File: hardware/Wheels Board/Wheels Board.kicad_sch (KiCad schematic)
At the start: 28 parts, among them J1 53307-2471, J2 MX150_02x04_Vertical, J4 Conn_01x08_Socket, U1 XIAO-ESP32-S3-SMD, U2 ASM330LHHTR, U5 TLV9002QDRQ1

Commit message: concepts of revA layout
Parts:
- removed J2: MX150_02x04_Vertical, UTSVT_Connectors:CONN_SD-75757-002_2X04_F16p09_MOL, symbol utsvt_connectors:MX150_02x04_Vertical
- removed J4: Conn_01x08_Socket, Connector_PinHeader_2.54mm:PinHeader_1x08_P2.54mm_Vertical, symbol Connector:Conn_01x08_Socket
- added J3: Conn_02x04_Counter_Clockwise, Connector_PinHeader_2.54mm:PinHeader_2x04_P2.54mm_Vertical, symbol Connector_Generic:Conn_02x04_Counter_Clockwise
- added J4: 757571121, mx150_2x2:CONN_SD-75757-002_2X02_F11p20_MOL, symbol mx150_2x2:757571121
- renumbered TP_GND2 to HALL_GND1, TP_OUT1 to HALL_OUT1, TP_5V2 to HALL_PWR1
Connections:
- net +24V: now also J4.1
- net CAN_H: now also J4.2
- net CAN_L: now also J4.3
- net ESP_SPI_CLK: now also J3.2 (Pin_2)
- net ESP_SPI_MISO: now also J3.4 (Pin_4)
- net ESP_SPI_MOSI: now also J3.3 (Pin_3)
- net ESP_SPI_SS: now also J3.1 (Pin_1)
- net GND: now also J4.4
- net IMU_SPI_CLK: now also J3.7 (Pin_7)
- net IMU_SPI_MISO: now also J3.5 (Pin_5)
- net IMU_SPI_MOSI: now also J3.6 (Pin_6)
- net IMU_SPI_SS: now also J3.8 (Pin_8)
- no-connect marks 22 -> 18
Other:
- note added: "MX150_CONNECTOR"
- note removed: "CONNECTOR"

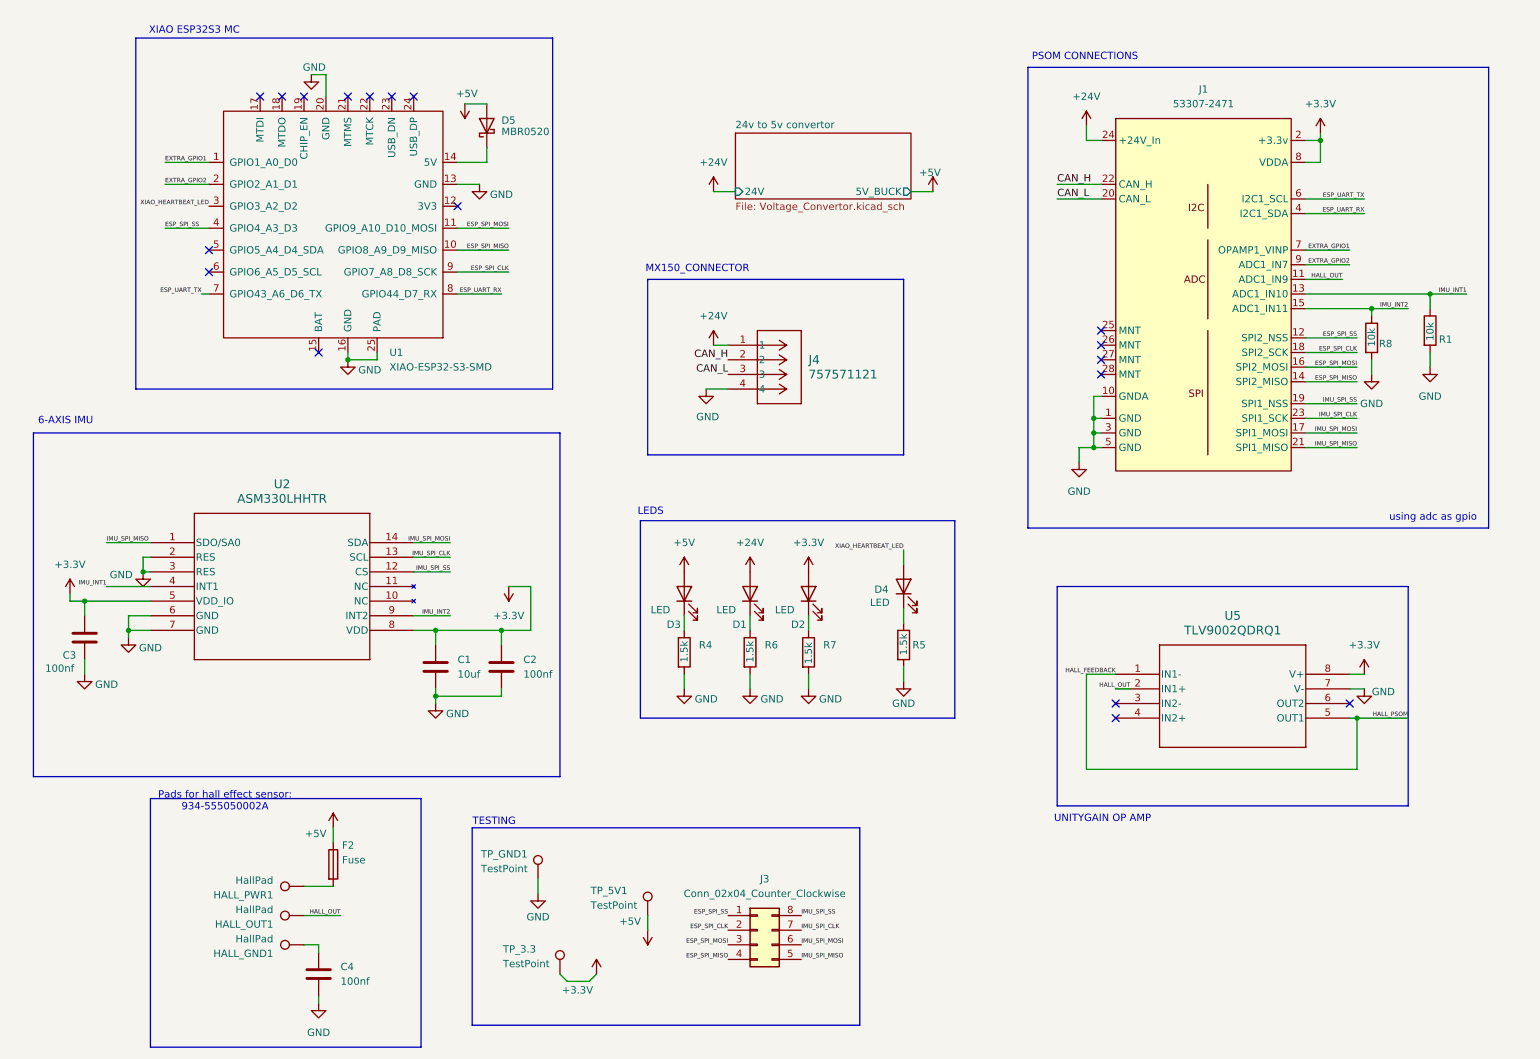
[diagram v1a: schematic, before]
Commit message: review council changes, layout not finalized
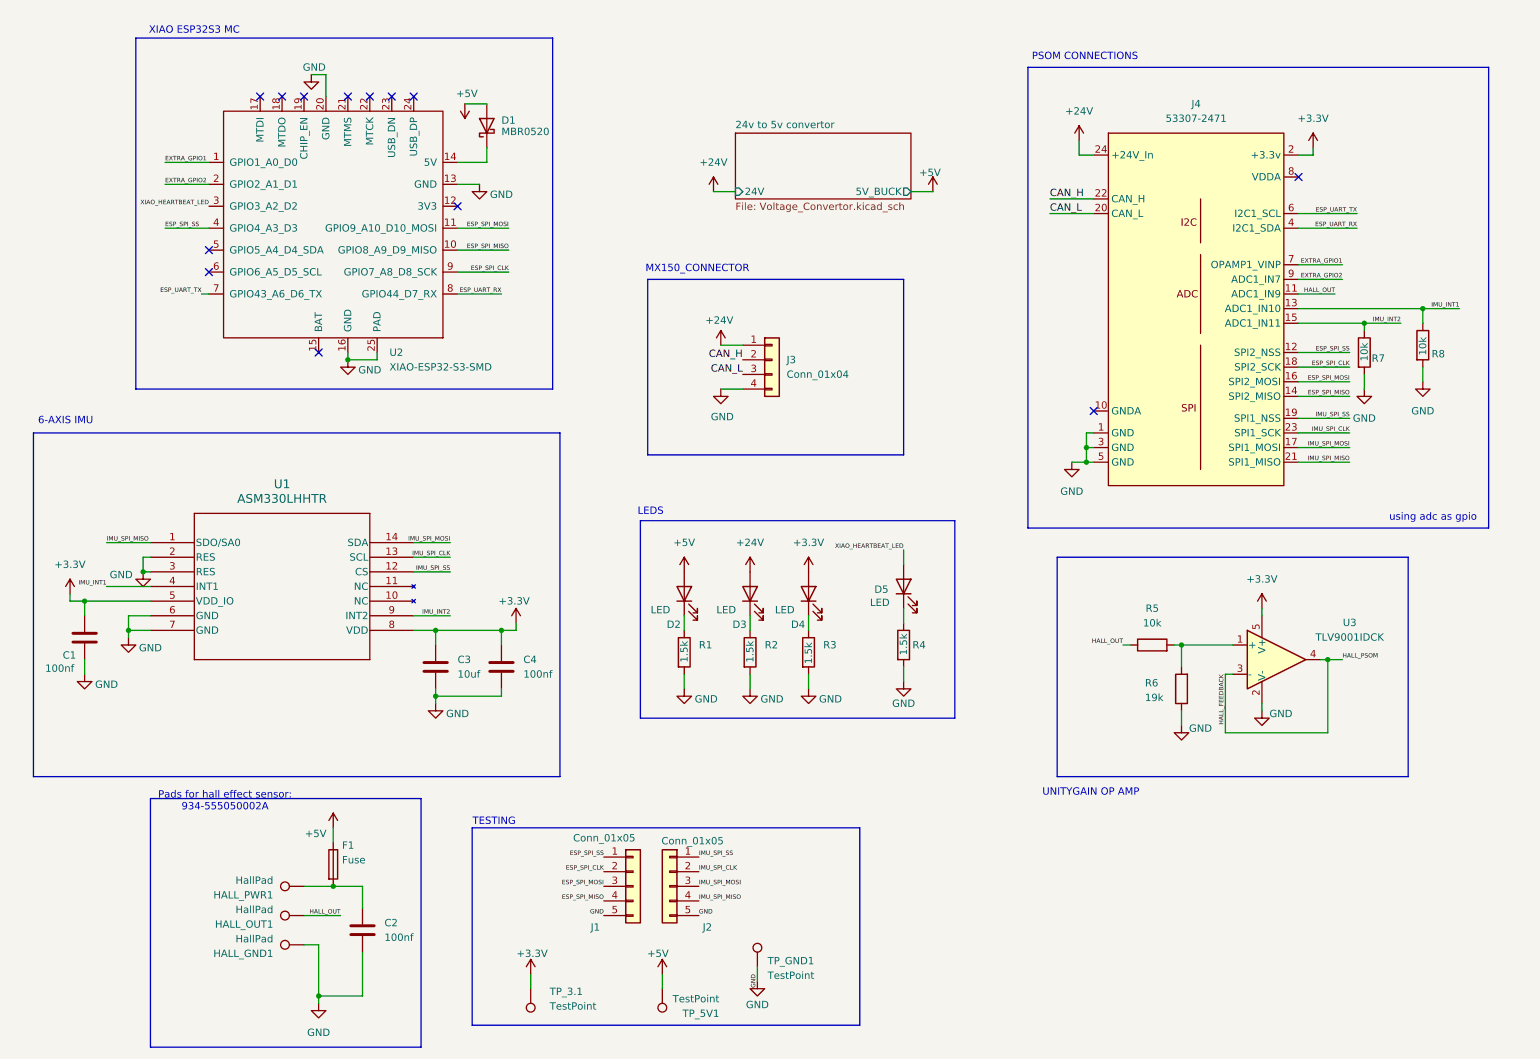
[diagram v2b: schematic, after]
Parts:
- removed C4: 100nf, Capacitor_SMD:C_0603_1608Metric_Pad1.08x0.95mm_HandSolder, symbol Device:C
- removed J1: 53307-2471, UTSVT_Connectors:PeripheralSOM, symbol utsvt_connectors:PeripheralSOMConnector
- removed J3: Conn_02x04_Counter_Clockwise, Connector_PinHeader_2.54mm:PinHeader_2x04_P2.54mm_Vertical, symbol Connector_Generic:Conn_02x04_Counter_Clockwise
- removed J4: 757571121, mx150_2x2:CONN_SD-75757-002_2X02_F11p20_MOL, symbol mx150_2x2:757571121
- removed R1: 10k, Resistor_SMD:R_0603_1608Metric_Pad0.98x0.95mm_HandSolder, symbol Device:R
- removed U5: TLV9002QDRQ1, TLV9002QDRQ1:SOIC8_D_TEX, symbol TLV9002QDRQ1(Op-Amp):TLV9002QDRQ1
- added C2: 100nf, Capacitor_SMD:C_0603_1608Metric_Pad1.08x0.95mm_HandSolder, symbol Device:C
- added J1, J2: Conn_01x05, Connector_PinHeader_1.00mm:PinHeader_1x05_P1.00mm_Vertical_SMD_Pin1Left, symbol Connector_Generic:Conn_01x05
- added J3: Conn_01x04, mx150_2x2:CONN_SD-75757-002_2X02_F11p20_MOL, symbol Connector_Generic:Conn_01x04
- added J4: 53307-2471, UTSVT_Connectors:PeripheralSOM, symbol utsvt_connectors:PeripheralSOMConnector
- added R5, R7: 10k, Resistor_SMD:R_0603_1608Metric_Pad0.98x0.95mm_HandSolder, symbol Device:R
- added R6: 19k, Resistor_SMD:R_0603_1608Metric_Pad0.98x0.95mm_HandSolder, symbol Device:R
- added U3: TLV9001IDCK, Package_TO_SOT_SMD:SOT-353_SC-70-5, symbol Amplifier_Operational:TLV9001IDCK
- C1: renamed from C3; P/N (none) -> MLASH168SB7104KTNA01
- C4: renamed from C2; P/N (none) -> MLASH168SB7104KTNA01
- D1: renamed from D5; P/N (none) -> MP01EA06
- U1: renamed from U2; P/N (none) -> ASM330LHHTR
- U2: renamed from U1; footprint XIAO-ESP32S3-SMD:XIAO-ESP32S3-SMD -> XIAO-ESP32S3:XIAO-ESP32S3-DIP; P/N (none) -> 113991114
- renumbered C1 to C3, D3 to D2, D1 to D3, D2 to D4, D4 to D5, F2 to F1, R4 to R1, R6 to R2, R7 to R3, R5 to R4, TP_3.3 to TP_3.1
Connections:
- net +24V: now also J3.1 (Pin_1), J4.24 (+24V_In)
- net +3.3V: now also J4.2 (+3.3v), U3.5 (V+)
- net CAN_H: now also J3.2 (Pin_2), J4.22 (CAN_H)
- net CAN_L: now also J3.3 (Pin_3), J4.20 (CAN_L)
- net ESP_SPI_CLK: now also J1.2 (Pin_2), J4.18 (SPI2_SCK)
- net ESP_SPI_MISO: now also J1.4 (Pin_4), J4.14 (SPI2_MISO)
- net ESP_SPI_MOSI: now also J1.3 (Pin_3), J4.16 (SPI2_MOSI)
- net ESP_SPI_SS: now also J1.1 (Pin_1), J4.12 (SPI2_NSS)
- net ESP_UART_RX: now also J4.4 (I2C1_SDA)
- net ESP_UART_TX: now also J4.6 (I2C1_SCL)
- net EXTRA_GPIO1: now also J4.7 (OPAMP1_VINP)
- net EXTRA_GPIO2: now also J4.9 (ADC1_IN7)
- net GND: now also HALL_GND1.1, C2.2, J1.5 (Pin_5), J2.5 (Pin_5), J3.4 (Pin_4), J4.1 (GND), J4.3 (GND), J4.5 (GND), R6.1, R7.2, U3.2 (V-)
- net HALL_FEEDBACK: now also U3.3 (-), U3.4
- net HALL_OUT: now also J4.11 (ADC1_IN9), R5.1
- net IMU_INT1: now also R8.1, J4.13 (ADC1_IN10)
- net IMU_INT2: now also J4.15 (ADC1_IN11), R7.1; no longer R8.1
- net IMU_SPI_CLK: now also J2.2 (Pin_2), J4.23 (SPI1_SCK)
- net IMU_SPI_MISO: now also J2.4 (Pin_4), J4.21 (SPI1_MISO)
- net IMU_SPI_MOSI: now also J2.3 (Pin_3), J4.17 (SPI1_MOSI)
- net IMU_SPI_SS: now also J2.1 (Pin_1), J4.19 (SPI1_NSS)
- net at F1.2, HALL_PWR1.1: now also C2.1
- new net: R5.2, R6.2, U3.1 (+)
- no-connect marks 18 -> 13
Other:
- moved on the sheet: TP_3.1, TP_5V1, TP_GND1

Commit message: pre wiring layout
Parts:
- HALL_GND1, HALL_OUT1, HALL_PWR1: footprint TestPoint:TestPoint_Pad_1.0x1.0mm -> Connector_PinHeader_2.54mm:PinHeader_1x01_P2.54mm_Vertical
- J1, J2: footprint Connector_PinHeader_1.00mm:PinHeader_1x05_P1.00mm_Vertical_SMD_Pin1Left -> Connector_PinHeader_1.00mm:PinHeader_1x05_P1.00mm_Vertical
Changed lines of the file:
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@@
 			)
 		)
-		(property "Footprint" "TestPoint:TestPoint_Pad_1.0x1.0mm"
+		(property "Footprint" "Connector_PinHeader_2.54mm:PinHeader_1x01_P2.54mm_Vertical"
 			(at 72.39 170.18 0)
 			(effects
@@
 			)
 		)
-		(property "Footprint" "TestPoint:TestPoint_Pad_1.0x1.0mm"
+		(property "Footprint" "Connector_PinHeader_2.54mm:PinHeader_1x01_P2.54mm_Vertical"
 			(at 72.39 160.02 0)
 			(effects
@@
 			)
 		)
-		(property "Footprint" "Connector_PinHeader_1.00mm:PinHeader_1x05_P1.00mm_Vertical_SMD_Pin1Left"
+		(property "Footprint" "Connector_PinHeader_1.00mm:PinHeader_1x05_P1.00mm_Vertical"
 			(at 129.54 165.1 0)
 			(effects
@@
 			)
 		)
-		(property "Footprint" "TestPoint:TestPoint_Pad_1.0x1.0mm"
+		(property "Footprint" "Connector_PinHeader_2.54mm:PinHeader_1x01_P2.54mm_Vertical"
 			(at 72.39 165.1 0)
 			(effects
@@
 			)
 		)
-		(property "Footprint" "Connector_PinHeader_1.00mm:PinHeader_1x05_P1.00mm_Vertical_SMD_Pin1Left"
+		(property "Footprint" "Connector_PinHeader_1.00mm:PinHeader_1x05_P1.00mm_Vertical"
 			(at 135.89 165.1 0)
 			(effects

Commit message: revised layout again
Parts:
- removed J3: Conn_01x04, mx150_2x2:CONN_SD-75757-002_2X02_F11p20_MOL, symbol Connector_Generic:Conn_01x04
- removed R5: 10k, Resistor_SMD:R_0603_1608Metric_Pad0.98x0.95mm_HandSolder, symbol Device:R
- removed R6: 19k, Resistor_SMD:R_0603_1608Metric_Pad0.98x0.95mm_HandSolder, symbol Device:R
- added J5: MX150_02x02_Vertical, UTSVT_Connectors:MX150_02x02_Vertical, symbol utsvt_connectors:MX150_02x02_Vertical
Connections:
- net +24V: now also J5.1 (+24V)
- net CAN_H: now also J5.2 (CANH_IN)
- net CAN_L: now also J5.4 (CANH_OUT)
- net GND: now also J5.3 (GND)
- net HALL_OUT: now also U3.1 (+)
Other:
- moved on the sheet: U3

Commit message: revised layout
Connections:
- net ESP_SPI_CLK: now also J1.4 (Pin_4); no longer J1.2 (Pin_2)
- net ESP_SPI_MISO: now also J1.2 (Pin_2); no longer J1.4 (Pin_4)
- net IMU_SPI_CLK: now also J2.1 (Pin_1); no longer J2.2 (Pin_2)
- net IMU_SPI_MISO: now also J2.2 (Pin_2); no longer J2.4 (Pin_4)
- net IMU_SPI_MOSI: now also J2.4 (Pin_4); no longer J2.3 (Pin_3)
- net IMU_SPI_SS: now also J2.3 (Pin_3); no longer J2.1 (Pin_1)
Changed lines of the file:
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@@
 	)
 	(label "ESP_SPI_CLK"
-		(at 124.46 162.56 180)
+		(at 124.46 167.64 180)
+		(effects
+			(font
+				(size 0.762 0.762)
+			)
+			(justify right bottom)
+		)
+	)
+	(label "ESP_SPI_SS"
+		(at 124.46 160.02 180)
 		(effects
 			(font
@@
 		)
 	)
+	(label "IMU_SPI_CLK"
+		(at 140.97 160.02 0)
+		(effects
+			(font
+				(size 0.762 0.762)
+			)
+			(justify left bottom)
+		)
+	)
 	(label "HALL_OUT"
 		(at 78.74 170.18 180)
@@
 		)
 	)
-	(label "IMU_SPI_MISO"
-		(at 140.97 167.64 0)
-		(effects
-			(font
-				(size 0.762 0.762)
-			)
-			(justify left bottom)
-		)
-	)
-	(label "IMU_SPI_CLK"
-		(at 140.97 162.56 0)
-		(effects
-			(font
-				(size 0.762 0.762)
-			)
-			(justify left bottom)
-		)
-	)
 	(label "ESP_SPI_MOSI"
 		(at 124.46 165.1 180)
@@
 		)
 	)
+	(label "ESP_SPI_MISO"
+		(at 124.46 162.56 180)
+		(effects
+			(font
+				(size 0.762 0.762)
+			)
+			(justify right bottom)
+		)
+	)
 	(label "IMU_INT2"
 		(at 262.89 67.31 180)
@@
 			)
 			(justify right bottom)
-		)
-	)
-	(label "IMU_SPI_MOSI"
-		(at 140.97 165.1 0)
-		(effects
-			(font
-				(size 0.762 0.762)
-			)
-			(justify left bottom)
 		)
 	)
@@
 		)
 	)
+	(label "IMU_SPI_MOSI"
+		(at 140.97 167.64 0)
+		(effects
+			(font
+				(size 0.762 0.762)
+			)
+			(justify left bottom)
+		)
+	)
 	(label "EXTRA_GPIO2"
 		(at 48.26 43.18 0)
@@
 			)
 			(justify right bottom)
+		)
+	)
+	(label "IMU_SPI_MISO"
+		(at 140.97 162.56 0)
+		(effects
+			(font
+				(size 0.762 0.762)
+			)
+			(justify left bottom)
 		)
 	)
@@
 		)
 	)
-	(label "ESP_SPI_SS"
-		(at 124.46 160.02 180)
-		(effects
-			(font
-				(size 0.762 0.762)
-			)
-			(justify right bottom)
-		)
-	)
 	(label "CAN_H"
 		(at 201.93 45.72 0)
@@
 		)
 	)
-	(label "ESP_SPI_MISO"
-		(at 124.46 167.64 180)
-		(effects
-			(font
-				(size 0.762 0.762)
-			)
-			(justify right bottom)
-		)
-	)
 	(label "IMU_SPI_MISO"
 		(at 254 91.44 180)
@@
 		)
 	)
+	(label "IMU_SPI_SS"
+		(at 140.97 165.1 0)
+		(effects
+			(font
+				(size 0.762 0.762)
+			)
+			(justify left bottom)
+		)
+	)
 	(label "HALL_OUT"
 		(at 251.46 62.23 180)
@@
 		)
 	)
-	(label "IMU_SPI_SS"
-		(at 140.97 160.02 0)
-		(effects
-			(font
-				(size 0.762 0.762)
-			)
-			(justify left bottom)
-		)
-	)

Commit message: final revisions!
i didnt do pn yet
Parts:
- removed HALL_GND1, HALL_OUT1, HALL_PWR1: HallPad, Connector_PinHeader_2.54mm:PinHeader_1x01_P2.54mm_Vertical, symbol Connector:TestPoint
- added J3: Conn_01x03, Connector_PinHeader_2.54mm:PinHeader_1x03_P2.54mm_Vertical, symbol Connector_Generic:Conn_01x03
- added LOGO1: LHRS, UTSVT_Logos:LHRs_LOGO, symbol utsvt_misc:Logo_Placeholder
- added LOGO2: cat, symbol utsvt_misc:Logo_Placeholder
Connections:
- net EXTRA_GPIO1: now also U2.2 (GPIO2_A1_D1); no longer U2.1 (GPIO1_A0_D0)
- net EXTRA_GPIO2: now also U2.3 (GPIO3_A2_D2); no longer U2.2 (GPIO2_A1_D1)
- net GND: now also J3.1 (Pin_1)
- net HALL_OUT: now also J3.2 (Pin_2)
- net XIAO_HEARTBEAT_LED: now also U2.1 (GPIO1_A0_D0); no longer U2.3 (GPIO3_A2_D2)
- net at C2.1, F1.2: now also J3.3 (Pin_3)
- net CAN_H renamed CAN_+
- net CAN_L renamed CAN_-
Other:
- note added: "GRAPHICS"
- moved on the sheet: C2, F1, U3
